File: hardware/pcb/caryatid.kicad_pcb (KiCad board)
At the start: 2 copper layers, 150 x 90 mm, 135 parts, among them J1 DC in, J10 FSR, J11 Digital bus, J12 RGB status, J13 Comms A - Qwiic, J14 Mic bias return, J15 Comms B - module, J16 Expansion / SPI1, J17 Audio out L/R/G, J18 Audio in L/R/rtn, J19 Comms A - module, J3 Latch switch, J4 Charge LEDs, J5 Analogue bus, J6 SW1 switch, J7 SW2 switch, J8 SW3 switch, J9 Soft pot, U1 BQ24074RGT, U2 TPS61023DRL, U3 74HC14, U4 MCP6002

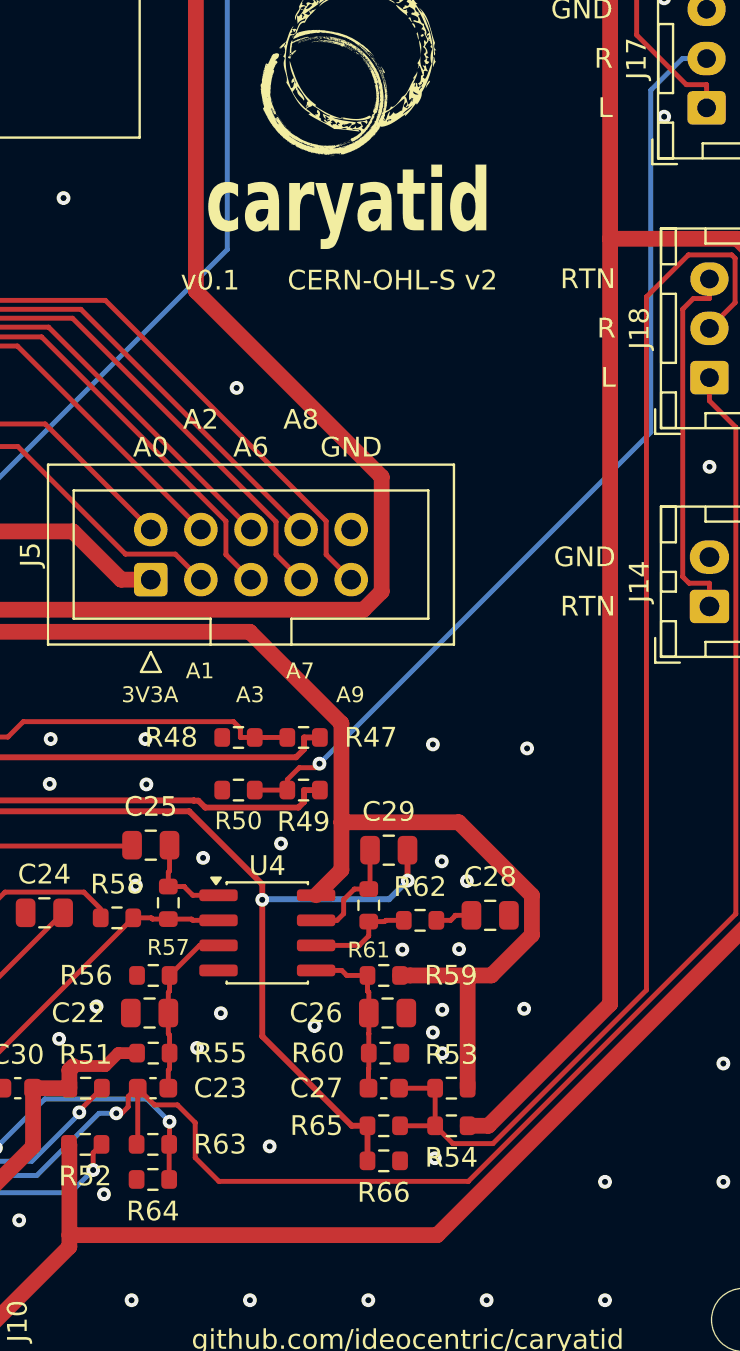
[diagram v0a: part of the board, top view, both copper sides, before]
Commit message: ADR 0010 step 2: update the board from the schematic; parity 28 -> 0
"Update PCB from Schematic" is a GUI menu item. kicad-cli 9.0.6 has no
equivalent and BOARD_NETLIST_UPDATER is not in the Python bindings
either, so this reproduces its effect through the pcbnew BOARD API. It
does NOT re-implement the updater: it applies one enumerated set of
changes, KiCad's own 28-item parity list, and touches nothing else.

  12  DNP cleared      C26-C29 R53 R54 R62 R65 R43-R46
   5  pads retargeted  C29.2 R53.2 R54.2 R62.2 R65.2
   3  values           JP1-3 gained the " L" suffix
   4  added            JP4 JP5 JP6 R68
   4  deleted          R48 R50 R64 R66

THE ACCEPTANCE TEST IS KiCad'S OWN AND IT IS EXACT: schematic parity
reports 0, down from 28. check_board 12/12. stale_tracks 0.

TWO DEFECTS THE DRY RUNS CAUGHT, BOTH OF THEM THE CASCADE THIS REPO KEEPS
RELEARNING -- a deleted or renetted pad takes routing with it.

  R48 WAS DNP BUT ITS PAD WAS COPPER, and the router had used it as the
  junction on /audio/OUT_L_J: R47.2 -- 170.8265 -- [R48.1 pad] --
  169.5163 -- west. Both stubs were load-bearing. Deleting them severed
  the net, and the signature was unmistakable: one unconnected item
  between two TRACKS with no pad involved. One 1.31 mm segment at the
  same width restores it, occupying the copper the pad used to.

  EIGHT STALE TRACKS on the five retargeted pads -- copper still arriving
  on the old net, which is a short between two nets that are now
  distinct. Six shorting_items before they were removed. Exactly what
  0491e70 found by hand on the left channel and what stale_tracks.py was
  written to find; now removed in the same pass that moves the pads.

ZONE REFILL IS NOT COSMETIC. Before it the GND pour still filled the
copper the new headers had landed in: 87 violations, 34
solder_mask_bridge + 20 clearance + 17 hole_clearance + 10
shorting_items, essentially all of them the plane touching new pads. It
is the B keystroke, and no DRC number means anything unti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
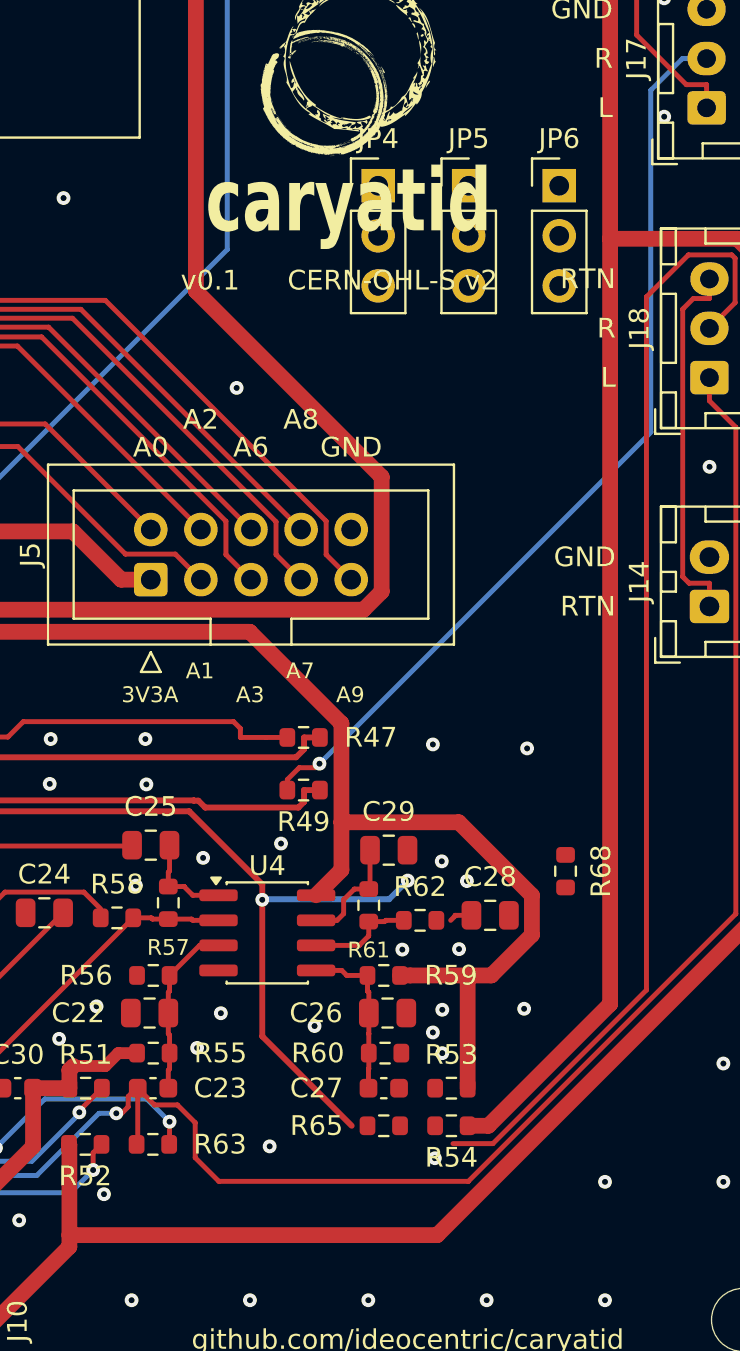
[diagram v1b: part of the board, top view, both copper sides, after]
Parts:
- removed R48, R50, R64, R66: open, Resistor_SMD:R_0603_1608Metric
- added JP4: Mic bias select R, Connector_PinHeader_2.54mm:PinHeader_1x03_P2.54mm_Vertical, F.Cu at (176.5, 57.5)
- added JP5: Mic path select R, Connector_PinHeader_2.54mm:PinHeader_1x03_P2.54mm_Vertical, F.Cu at (181.1, 57.5)
- added JP6: Mic gain select R, Connector_PinHeader_2.54mm:PinHeader_1x03_P2.54mm_Vertical, F.Cu at (185.7, 57.5)
- added R68: 392R, Resistor_SMD:R_0603_1608Metric, F.Cu at (186.0, 92.2)
- JP1: value Mic bias select -> Mic bias select L
- JP2: value Mic path select -> Mic path select L
- JP3: value Mic gain select -> Mic gain select L
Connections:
- C29 pad 2: AUDIO_IN_R -> AMP_OUT_R
- R53 pad 2: /audio/MIC_R -> /audio/BIAS_E_R
- R54 pad 2: /audio/MIC_R -> /audio/BIAS_C_R
- R62 pad 2: /audio/GAINLEG_R -> /audio/LEG_101_R
- R65 pad 2: AUDIO_IN_R -> BYPASS_R
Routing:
- net /audio/MIC_R: track 64.5 -> 57.7 mm
- net AUDIO_IN_R: track 63.9 -> 59.8 mm
- net BYPASS_L: track 24.1 -> 22.3 mm
- net /audio/OUT_R_J: track 48.7 -> 47.1 mm
- net /audio/GAINLEG_R: track 1.90 -> 1.17 mm

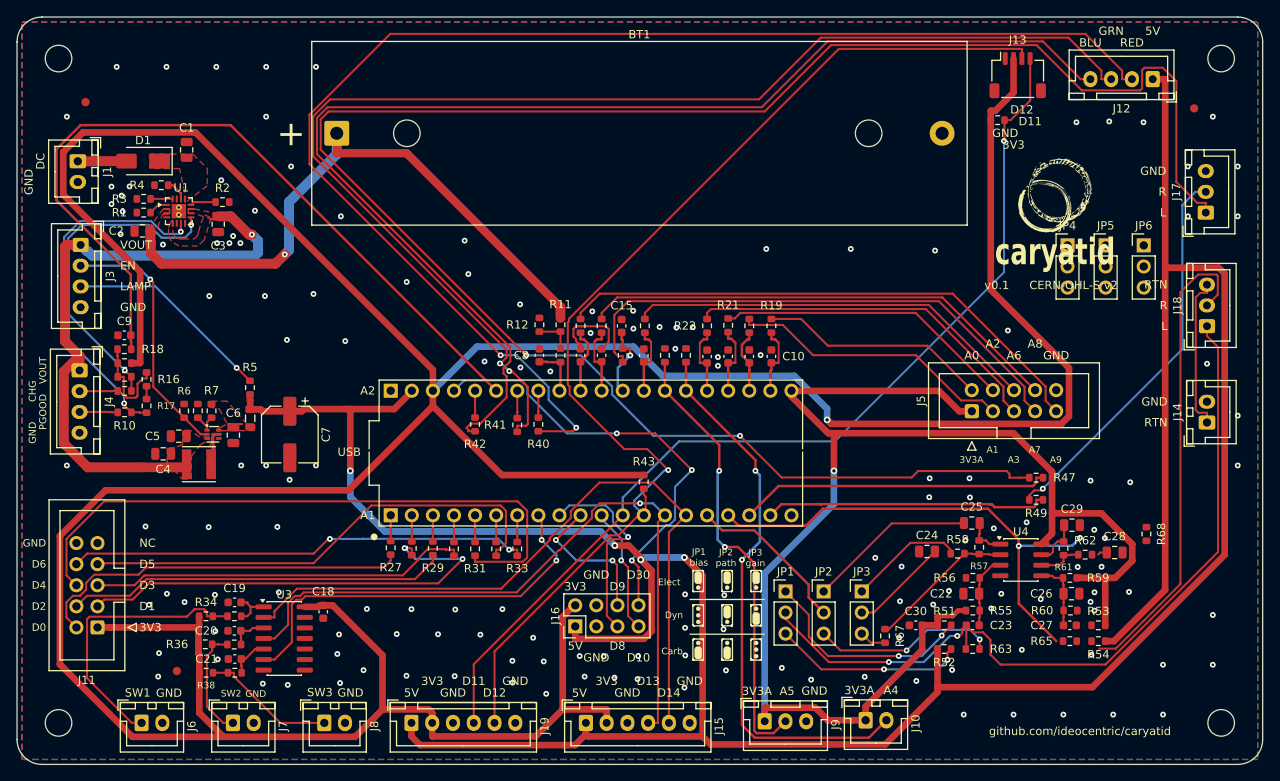
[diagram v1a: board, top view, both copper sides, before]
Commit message: Strip all routing and zone fills; keep the placement, start the route again
949 tracks (4324 mm of copper) and 203 vias removed, all 10 zones
unfilled. Nothing else touched.

WHY, AND IT IS NOT DISSATISFACTION WITH THE ROUTE. The routed board had
no room where it needed it: ADR 0010's right-channel jumpers could not
be placed within 41.6 mm of the circuitry they select, measured against
every courtyard, pad, via and track, while the upper board sat largely
empty. Patching around that means long analogue runs to a trio of
jumpers parked across the board. Re-routing from a rebalanced placement
is cheaper than defending a layout that is full in the wrong place.

WHAT SURVIVES IS THE WHOLE POINT, so it is asserted rather than assumed.
The script fingerprints every footprint before and after -- position,
orientation, schematic `path`, value, DNP flag and every pad's net --
and refuses to write if any of them differs. 135 footprints, unchanged.
The uuids matter most: a lost `path` silently orphans a part from the
netlist and the BOM, and nothing downstream would say so.

Also kept: the 10 zone OUTLINES. Only two are ground fill; the other
eight are the hand-drawn power pours ADR 0008 uses AS ROUTING for VBAT,
VOUT, +5V_RAW, VIN_DC and SW. They are kept because deleting them is one
click and redrawing them is not -- NOT because they stay correct. They
are shaped around where U1 and U2 sit today and go stale the moment
those parts move.

VERIFIED:

  schematic parity   0        routing is not part of parity, so this
                              moving would have meant structural damage
  unconnected      263        the full ratsnest, and it is the SAME
                              number hardware/pcb/README.md records for
                              this board before it was ever routed
  check_board     12/12
  segments/vias/fills in the file: 0 / 0 / 0

Still reported, and both pre-existing: 5 lib_footprint_mismatch, the
accepted exclusions, and 23 silkscreen items fro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
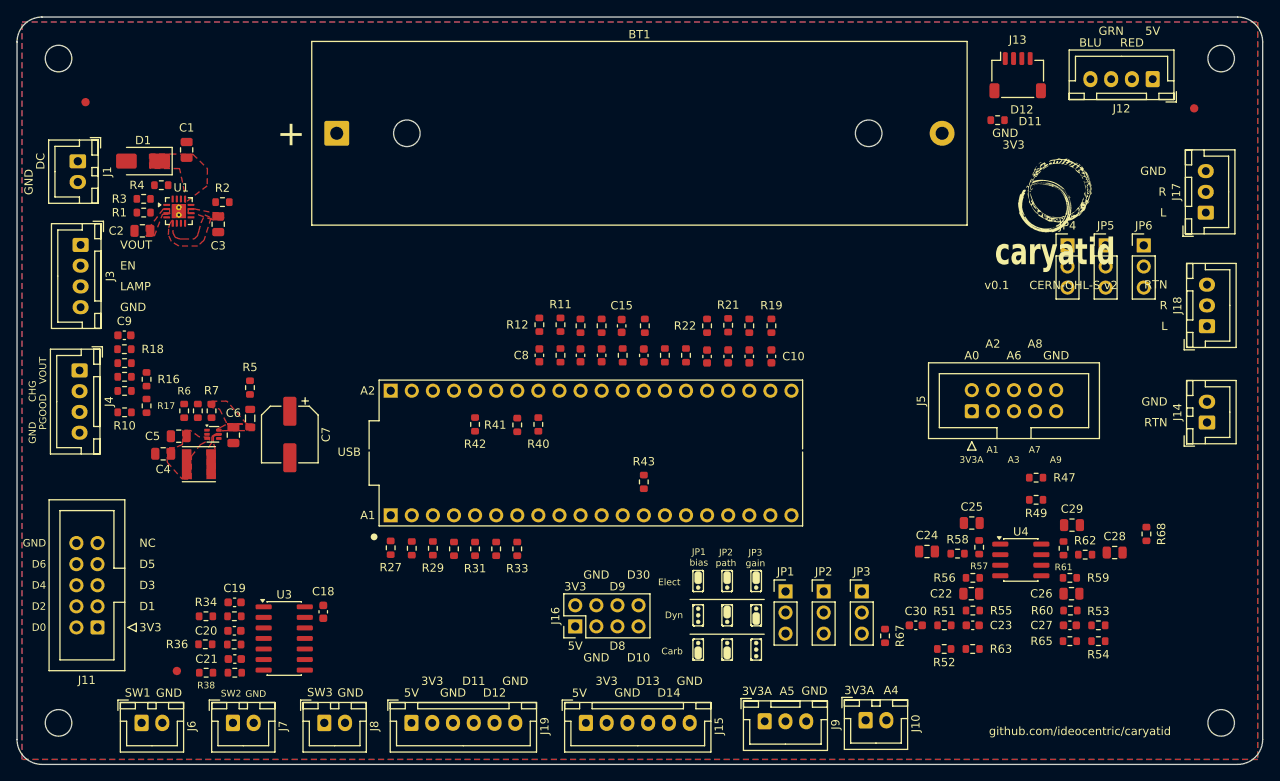
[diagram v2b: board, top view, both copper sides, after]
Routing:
- net +3V3: track 456.3 -> 0.00 mm, vias 1 -> 0
- net +5V: track 350.3 -> 0.00 mm, vias 4 -> 0
- net /audio/OUT_L_J: track 236.8 -> 0.00 mm, vias 2 -> 0
- net +3V3A: track 167.6 -> 0.00 mm, vias 1 -> 0
- net /panel-io/RGB_R: track 162.8 -> 0.00 mm, vias 2 -> 0
- net /panel-io/RGB_G: track 153.6 -> 0.00 mm, vias 2 -> 0
- net /panel-io/RGB_B: track 150.3 -> 0.00 mm
- net D12: track 138.6 -> 0.00 mm, vias 1 -> 0
- net D11: track 119.2 -> 0.00 mm, vias 1 -> 0
- net /audio/MIC_L: track 96.4 -> 0.00 mm, vias 2 -> 0
- net A11: track 95.2 -> 0.00 mm
- net D14: track 86.1 -> 0.00 mm
- net D13: track 84.2 -> 0.00 mm, vias 1 -> 0
- net /panel-io/D4_S: track 76.7 -> 0.00 mm
- net VBAT: track 75.3 -> 0.00 mm, vias 1 -> 0
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
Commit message: Re-place the 77 pin labels for the new placement, and drop ten orphans
Placement moved 92 of 135 footprints; the silkscreen did not follow,
because the pin labels are standalone board text at absolute coordinates
rather than footprint fields. 107 silk_overlap and 15 silk_over_copper.

  pin_labels.py --relock --apply    107 -> 46
  drop_orphan_pin_labels.py          46 -> 25

--relock rather than --apply, because faea30a had LOCKED every label to
stop re-runs reverting hand nudges, and a plain --apply skips locked
ones. That protection was doing its job and was the reason the labels
could not be selected in the editor either. They are unlocked again now,
so they can be dragged; `pin_labels.py --lock --apply` puts the
protection back once placement settles.

TEN LABELS WERE UNREACHABLE IN BOTH DIRECTIONS, AND HAD BEEN FOR SIX
COMMITS. pin_labels derives each uuid from its connector's NAME:

    uuid5(NS, f"caryatid-pinlabel-{ref}-{pin}")

276149a renamed J13A -> J13 and J13B -> J19. The labels on the board kept
uuids computed from the old names, so the tool stopped owning them: never
stripped, never regenerated, never moved. faea30a then locked every
label, which sealed it -- --relock only forces the strip of labels the
tool KNOWS about.

They were not duplicates until today, which is why nothing looked wrong.
They were the ONLY labels J13 and J19 had, the board rendered correctly
and the count came out right. Regenerating produced the real ones and
only then did the orphans become a second set at stale coordinates: J19
carrying 11 labels for six pins, J13's four stranded 6 mm from where J13
now sits. On a fabricated board that is ink naming the wrong pins.

Removed by explicit uuid, ten named individually, because the general
rule -- locked, looks like a pin label, unowned -- would also match any
hand-placed text somebody deliberately locked.

TWO FIXES THIS EARNS, neither of which belongs in a one-shot: a rename
should re-key its labels, or the uuid should not enco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
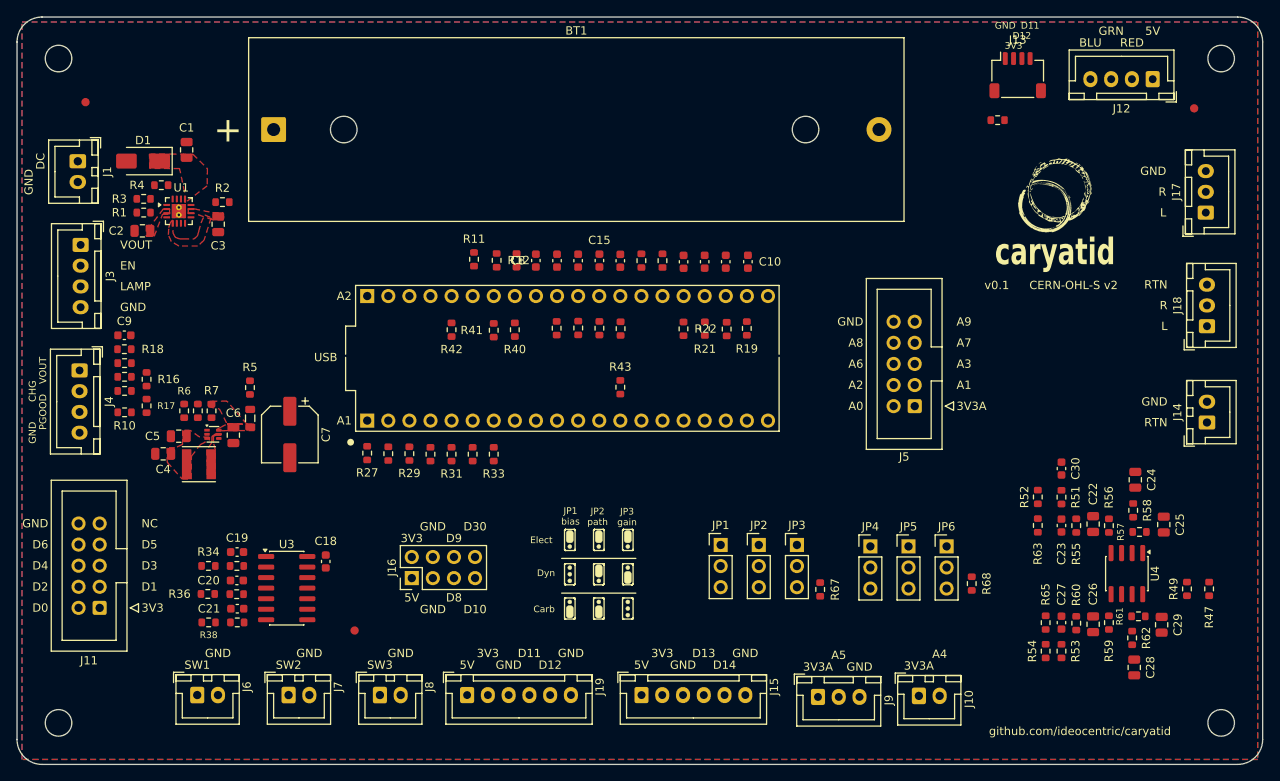
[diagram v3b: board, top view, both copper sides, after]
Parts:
- moved JP4 43.3 mm to (152.8, 93.7)
- moved JP5 43.3 mm to (157.3, 93.7)
- moved JP6 43.3 mm to (161.9, 93.7)
- moved C24 26.5 mm to (184.7, 85.7), turned to 90 degrees
- moved C30 25.8 mm to (175.8, 84.4), turned to 90 degrees
- moved R47 24.8 mm to (193.6, 98.9), turned to 90 degrees
- moved C25 23.1 mm to (188.1, 91.1), turned to 90 degrees
- moved FID3 21.9 mm to (90.7, 103.9)
- moved R68 21.9 mm to (165.0, 98.2)
- moved R58 21.8 mm to (184.4, 89.4), turned to 90 degrees
- moved R52 21.5 mm to (172.9, 87.8), turned to -90 degrees
- moved R49 21.1 mm to (190.9, 98.9), turned to 90 degrees
- moved R51 20.9 mm to (175.8, 87.8), turned to -90 degrees
- moved J16 20.5 mm to (97.5, 97.6)
- moved R57 19.4 mm to (185.2, 92.0), turned to 0 degrees
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
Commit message: Placement tweaks: nine parts onto grid, FID3 moved clear
Nine sub-millimetre nudges (R11, R20-R22, R40, R41, R43, R67, C10)
settling parts onto the grid, and FID3 moved 31.3 mm to (61.42, 115.12).

Committed before the Freerouting run so the route arrives as its own diff
against a known placement, rather than mixed in with hand edits.
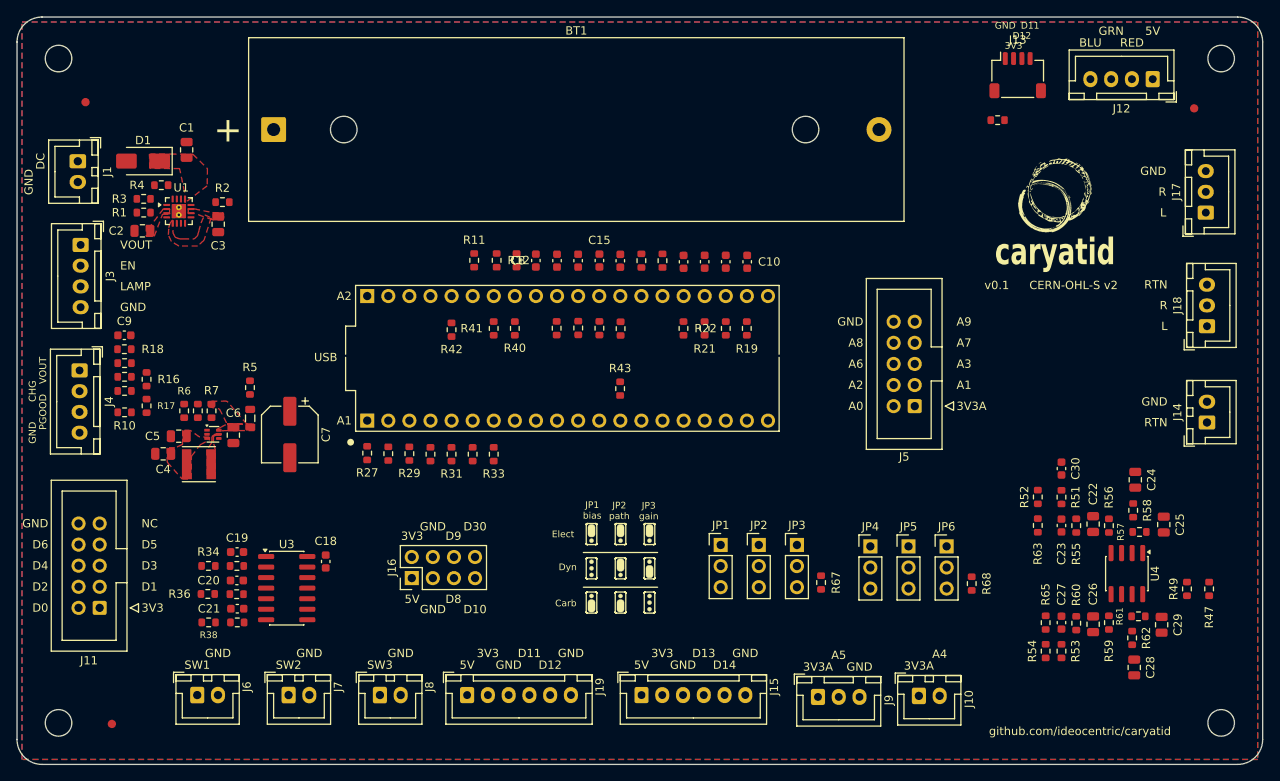
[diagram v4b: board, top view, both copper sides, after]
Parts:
- moved FID3 31.3 mm to (61.4, 115.1)
- moved R67 0.84 mm to (146.8, 98.1)
- moved R41 0.22 mm to (107.4, 67.5)
- moved R43 0.17 mm to (122.6, 74.8)
- moved R40 0.16 mm to (109.9, 67.5)
- moved R20 0.13 mm to (135.3, 67.5)
- moved R11 0.13 mm to (105.0, 59.3)
- moved C10 0.09 mm to (137.9, 59.5)
